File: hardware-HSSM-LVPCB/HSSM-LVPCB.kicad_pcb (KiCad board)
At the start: 2 copper layers, 42 x 12 mm, 57 parts, among them J1 UFL_R_SMT_1_10, J2 LPPB061NGCN-RC, Q1 Q_MOSFET_N_BSS123, Q2 Q_MOSFET_N_BSS123, U1 ESP32-C6, U2 W25Q64JVSSIQ_SOIC-8, X1 X_40MHz_SMD_ECS-2520SMV-400-F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

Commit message: [#9] PCB placement WIP
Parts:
- C4: moved to F.Cu
- moved C4 30.7 mm to (149.9, 115.8)
- moved C5 18.5 mm to (156.4, 116.0), turned to -90 degrees
- moved C16 15.8 mm to (125.1, 105.3)
- moved C17 15.8 mm to (127.1, 105.3)
- moved R12 15.8 mm to (125.8, 106.3)
- moved R16 15.8 mm to (122.9, 100.3)
- moved C18 15.8 mm to (126.5, 107.7)
- moved C19 15.8 mm to (119.3, 107.4)
- moved R11 15.8 mm to (125.8, 104.3)
- moved R13 15.8 mm to (121.5, 103.0)
- moved R14 15.8 mm to (119.2, 101.0)
- moved R15 15.8 mm to (122.9, 98.4)
- moved R17 15.8 mm to (122.9, 102.3)
- moved C3 8.54 mm to (147.9, 117.0), turned to -90 degrees
- moved Q1 7.44 mm to (152.1, 109.9)
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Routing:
- net /BOOT: track 2.98 -> 0.00 mm
- net /DTR: track 1.26 -> 0.00 mm, vias 1 -> 0

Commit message: [#9] PCB placement WIP
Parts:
- C7: moved to F.Cu
- moved C7 26.6 mm to (148.9, 115.2)
- moved C6 17.0 mm to (153.4, 115.5), turned to 180 degrees
- moved Q2 9.81 mm to (147.9, 109.4)
- moved C5 5.43 mm to (151.1, 114.8)
- moved X1 2.00 mm to (146.8, 122.4)
- moved C14 2.00 mm to (144.6, 122.3)
- moved C13 1.65 mm to (149.0, 122.3), turned to 90 degrees
- moved C4 1.20 mm to (149.9, 114.6)
- moved L2 1.02 mm to (149.9, 116.5)
- moved C3 0.96 mm to (148.9, 117.1)
- moved R7 0.61 mm to (147.5, 120.4), turned to 0 degrees
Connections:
- U1 pad 19: unconnected-(U1-GPIO13-Pad19) -> /GPIO3
- U1 pad 9: /GPIO3 -> unconnected-(U1-GPIO3-Pad9)
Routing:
- net /GPIO0: track 0.00 -> 3.39 mm
- net Net-(U1-VDDPST1): track 0.00 -> 2.67 mm
- net /GPIO1: track 0.00 -> 2.63 mm
- net /GPIO2: track 0.00 -> 2.13 mm
- net +3V3: track 0.00 -> 1.53 mm, vias 0 -> 2
- net /Enable: track 0.00 -> 1.36 mm, vias 0 -> 1

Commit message: [#9] PCB placement WIP
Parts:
- C11: moved to F.Cu
- moved R22 12.2 mm to (145.8, 112.8), turned to 180 degrees
- moved C12 11.2 mm to (150.3, 122.4), turned to 90 degrees
- moved C11 8.25 mm to (148.8, 120.1), turned to 180 degrees
- moved R7 0.61 mm to (146.9, 120.5)
- moved C14 0.48 mm to (144.1, 122.3), turned to 0 degrees
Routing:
- net +3V3: track 1.53 -> 6.57 mm

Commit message: [#9] PCB placement WIP
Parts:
- C10, C18, C8, R1, R10, R11, R12, R13, R16, R2, R3, R4, R5, R6, R8, R9: moved to F.Cu
- moved R16 36.5 mm to (156.7, 114.1), turned to 45 degrees
- moved D2 33.3 mm to (153.6, 113.3)
- moved D7 33.2 mm to (120.4, 113.2)
- moved Q2 33.0 mm to (119.9, 126.8), turned to 90 degrees
- moved Q1 31.6 mm to (125.3, 126.7), turned to 90 degrees
- moved R19 29.9 mm to (151.3, 112.7), turned to 0 degrees
- moved C18 28.1 mm to (153.8, 114.4)
- moved R1 24.2 mm to (138.8, 128.1)
- moved R2 22.9 mm to (138.8, 126.8)
- moved U2 21.0 mm to (134.1, 127.4)
- moved R8 18.9 mm to (134.2, 130.7)
- moved R6 16.4 mm to (139.7, 118.1), turned to 180 degrees
- moved R13 14.0 mm to (127.8, 115.6), turned to 90 degrees
- moved R3 14.0 mm to (129.4, 128.0), turned to 0 degrees
- moved C10 13.8 mm to (140.1, 117.1), turned to 0 degrees
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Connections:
- C8 pad 2: Net-(U1-VDD_SPI) -> VDD_SPI
- C9 pad 2: Net-(U1-VDD_SPI) -> VDD_SPI
- U1 pad 23: Net-(U1-VDD_SPI) -> VDD_SPI
- U2 pad 8: +3V3 -> VDD_SPI
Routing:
- net /RTS: track 0.00 -> 7.83 mm
- net Net-(Q2-G): track 0.00 -> 3.86 mm
- net /DTR: track 0.00 -> 2.30 mm
- net Net-(Q1-G): track 0.00 -> 1.35 mm

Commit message: [#9] PCB placement
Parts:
- C16, C17, C19, R14, R15, R17: moved to F.Cu
- moved R17 20.6 mm to (138.8, 115.4), turned to -90 degrees
- moved C19 20.4 mm to (138.8, 113.5)
- moved Q2 19.6 mm to (138.6, 120.8), turned to -90 degrees
- moved R14 17.5 mm to (128.9, 115.6), turned to 90 degrees
- moved R10 16.7 mm to (135.9, 118.7), turned to 0 degrees
- moved R15 16.7 mm to (121.7, 115.0), turned to -90 degrees
- moved R9 15.6 mm to (135.9, 119.7), turned to 180 degrees
- moved R20 15.2 mm to (136.4, 121.2), turned to -90 degrees
- moved R21 13.3 mm to (135.4, 121.2), turned to -90 degrees
- moved C16 13.3 mm to (130.3, 117.6), turned to 180 degrees
- moved C9 11.7 mm to (122.2, 122.9)
- moved C8 11.7 mm to (120.9, 121.2)
- moved U2 11.7 mm to (125.6, 119.3)
- moved R2 11.7 mm to (130.3, 118.7)
- moved R3 11.7 mm to (120.9, 119.9)
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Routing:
- net +3V3: track 6.68 -> 2.11 mm
- net Net-(U1-SPIHD): track 0.00 -> 0.59 mm, vias 0 -> 1
- net Net-(U1-SPID): track 0.00 -> 0.59 mm, vias 0 -> 1
- net Net-(U1-SPICLK): track 0.00 -> 0.59 mm, vias 0 -> 1
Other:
- board size 42 x 12 mm -> 36 x 12 mm

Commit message: [#13] PCB routing WIP flash
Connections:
- R8 pad 2: +3V3 -> VDD_SPI
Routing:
- net VDD_SPI: track 0.00 -> 5.77 mm, vias 0 -> 1
- net /GPIO3: track 0.00 -> 4.50 mm
- net /SPICS0: track 0.00 -> 2.57 mm
- net /SPIQ: track 0.00 -> 1.85 mm
- net /SPIWP: track 0.00 -> 1.73 mm
- net /SPIHD: track 0.00 -> 1.73 mm
- net /SPICLK: track 0.00 -> 1.73 mm
- net /SPID: track 0.00 -> 1.72 mm
- net GND: track 0.00 -> 1.60 mm, vias 0 -> 2
- net Net-(D6-Pad4): track 0.00 -> 1.52 mm
- net +3V3: track 2.11 -> 3.63 mm
- net Net-(D6-Pad3): track 0.00 -> 1.13 mm
- net Net-(D6-Pad2): track 0.00 -> 1.13 mm
- net Net-(U1-SPIWP): track 0.00 -> 0.97 mm, vias 0 -> 1
- net Net-(U1-SPIQ): track 0.00 -> 0.89 mm, vias 0 -> 1

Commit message: [#13] PCB routing WIP
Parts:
- moved C16 2.28 mm to (129.2, 115.6), turned to -90 degrees
- moved R14 0.70 mm to (128.2, 115.6)
- moved R13 0.60 mm to (127.2, 115.6)
- moved D6 0.55 mm to (126.7, 113.7)
- moved R11 0.50 mm to (126.2, 115.6)
- moved R12 0.40 mm to (125.2, 115.6)
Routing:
- net GND: track 1.60 -> 5.16 mm, vias 2 -> 3
- net /GPIO0: track 3.39 -> 5.36 mm, vias 0 -> 1
- net /GPIO1: track 2.63 -> 4.45 mm, vias 0 -> 1
- net /GPIO3: track 4.50 -> 5.94 mm, vias 0 -> 1
- net /GPIO2: track 2.13 -> 3.33 mm, vias 0 -> 1

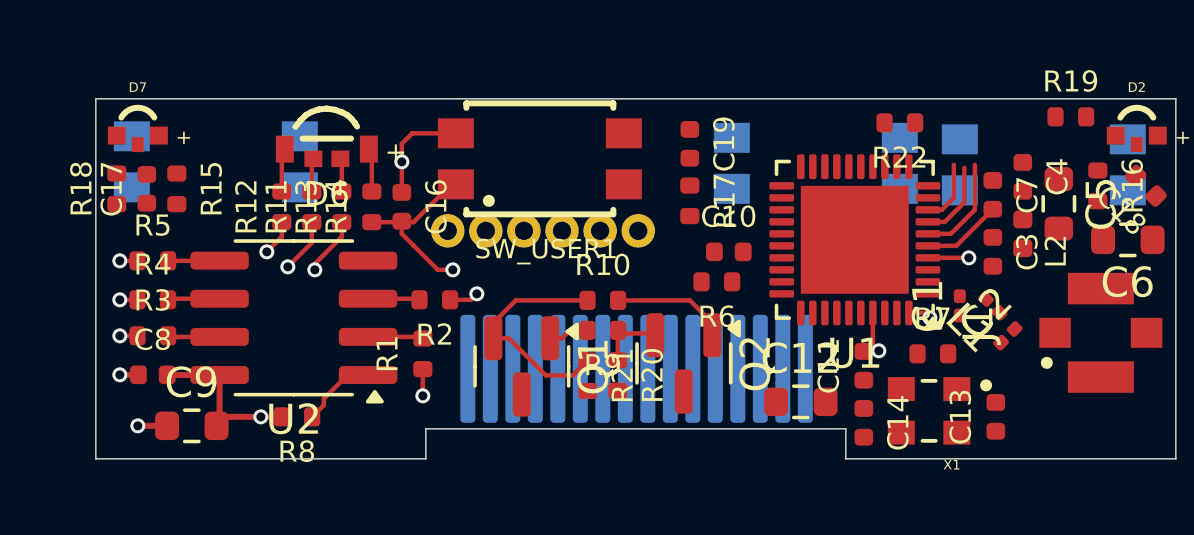
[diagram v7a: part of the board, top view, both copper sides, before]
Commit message: [#13] PCB routing WIP ESP32-C6
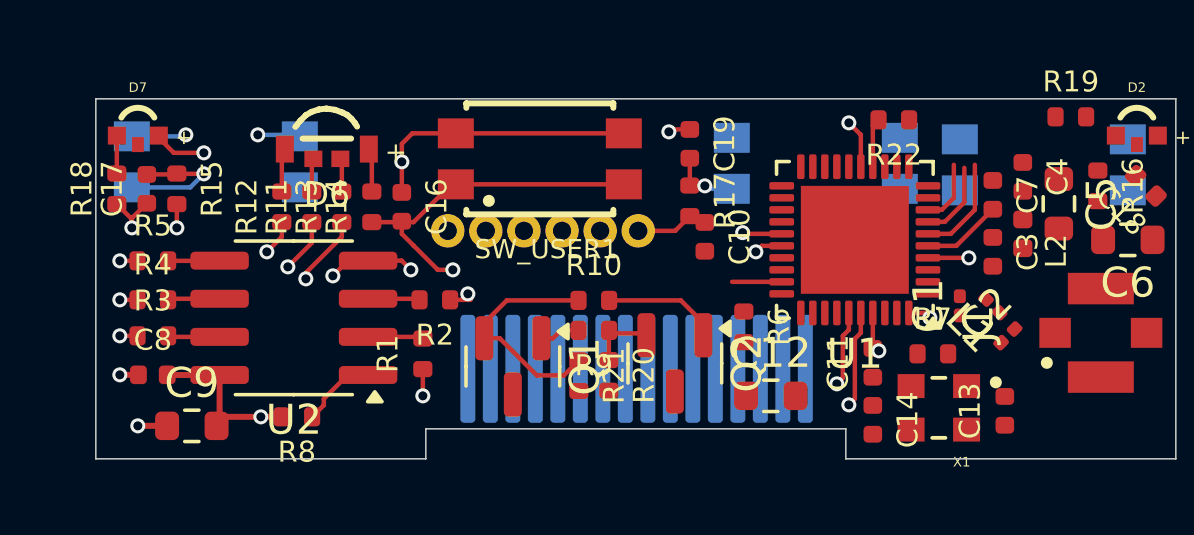
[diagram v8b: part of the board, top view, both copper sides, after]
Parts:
- moved R6 1.75 mm to (140.6, 119.6), turned to -90 degrees
- moved C12 1.02 mm to (141.5, 121.9)
- moved C10 0.94 mm to (139.3, 116.6), turned to -90 degrees
- moved C13 0.36 mm to (149.3, 122.4)
- moved X1 0.34 mm to (147.1, 122.3)
- moved C11 0.32 mm to (144.9, 120.8)
- moved C14 0.32 mm to (144.9, 122.7)
- moved R10 0.30 mm to (135.6, 118.7)
- moved R20 0.30 mm to (136.1, 121.2)
- moved R21 0.30 mm to (135.1, 121.2)
- moved R9 0.30 mm to (135.6, 119.7)
- moved Q1 0.30 mm to (132.9, 120.9)
- moved Q2 0.30 mm to (138.3, 120.8)
- moved R22 0.22 mm to (145.6, 112.7)
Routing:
- net GND: track 5.16 -> 19.7 mm, vias 3 -> 9
- net /GPIO3: track 5.94 -> 11.5 mm
- net /GPIO23: track 0.00 -> 5.58 mm, vias 0 -> 2
- net /GPIO21: track 0.00 -> 4.50 mm, vias 0 -> 1
- net +3V3: track 3.57 -> 6.28 mm, vias 2 -> 3
- net /GPIO22: track 0.00 -> 2.53 mm, vias 0 -> 1
- net /GPIO_Q1: track 0.00 -> 1.78 mm, vias 0 -> 1
- net Net-(U1-U0TXD): track 0.00 -> 1.65 mm
- net /GPIO8: track 0.00 -> 1.64 mm
- net /BOOT: track 0.00 -> 1.63 mm, vias 0 -> 1
- net Net-(U1-SPICLK): track 0.59 -> 1.91 mm, vias 1 -> 2
- net Net-(D7-Pad1): track 0.00 -> 1.27 mm
- net Net-(U1-SPID): track 0.59 -> 1.54 mm, vias 1 -> 2
